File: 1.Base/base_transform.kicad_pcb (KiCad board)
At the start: 2 copper layers, 20 x 22.6 mm, 0 parts

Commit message: Updated Base File
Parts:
- added REF**: FBConnector, 1.Cookie.Board:FBConnector, F.Cu at (26.4, 23.8)
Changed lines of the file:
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@@
   )
   (net 0 "")
+  (footprint "1.Cookie.Board:FBConnector" (layer "F.Cu")
+    (at 26.35 23.79)
+    (fp_text reference "REF**" (at -0.02 9.21 unlocked) (layer "F.SilkS") hide
+        (effects (font (size 1 1) (thickness 0.1)))
+    )
+    (fp_text value "FBConnector" (at 0.36 13.61 unlocked) (layer "F.Fab") hide
+        (effects (font (size 1 1) (thickness 0.15)))
+    )
+    (fp_rect (start -0.1 -0.1) (end 0.1 0.1)
+      (stroke (width 0.01) (type solid)) (fill solid) (layer "F.Cu"))
+    (fp_rect (start -0.1 -0.1) (end 0.1 0.1)
+      (stroke (width 0.01) (type solid)) (fill solid) (layer "B.Cu"))
+    (pad "1" thru_hole circle (at 0 0) (size 0.1 0.1) (drill 0.1) (layers "*.Cu"))
+  )
   (gr_arc (start 26.83504 32.235) (mid 27.194224 32.383804) (end 27.34304 32.743)
     (stroke (width 0.1) (type solid)) (layer "F.Cu"))
@@
     )
     (stroke (width 0.1) (type solid)) (fill solid) (layer "F.Cu"))
-  (gr_arc (start 25.93 22.93) (mid 29.012419 27.568262) (end 30.552985 32.920032)
-    (stroke (width 0.5) (type solid)) (layer "F.Cu"))
   (gr_arc (start 32.44844 34.2416) (mid 32.299653 34.600824) (end 31.94044 34.7496)
     (stroke (width 0.1) (type solid)) (layer "F.Cu"))
@@
     )
     (stroke (width 0.1) (type solid)) (fill solid) (layer "B.Cu"))
+  (gr_line (start 26.35 23.79) (end 31 28.44)
+    (stroke (width 0.2) (type default)) (layer "B.Cu"))
   (gr_poly
     (pts
@@
   (gr_arc (start 13.014724 32.743379) (mid 13.163522 32.384177) (end 13.522724 32.235379)
     (stroke (width 0.1) (type solid)) (layer "B.Cu"))
+  (gr_line (start 31 28.44) (end 31 32.82)
+    (stroke (width 0.2) (type default)) (layer "B.Cu"))
   (gr_poly
     (pts
@@
     )
     (stroke (width 0.1) (type solid)) (fill solid) (layer "B.Cu"))
-  (gr_arc (start 26.255922 12.500319) (mid 22.70698 16.050122) (end 19.154081 12.504279)
-    (stroke (width 0.01) (type solid)) (layer "F.SilkS"))
   (gr_rect (start 12.435 32.085) (end 32.815 35.245)
     (stroke (width 0.01) (type solid)) (fill solid) (layer "B.Mask"))
-  (gr_rect (start 16.955 25.895) (end 26.455 16.095)
-    (stroke (width 0.01) (type solid)) (fill solid) (layer "F.Mask"))
-  (gr_rect (start 12.435 32.085) (end 32.815 35.245)
+  (gr_rect (start 12.61 12.47) (end 32.7 35.231967)
     (stroke (width 0.01) (type solid)) (fill solid) (layer "F.Mask"))
   (gr_line (start 29.4233 35.1052) (end 32.29604 35.1052)

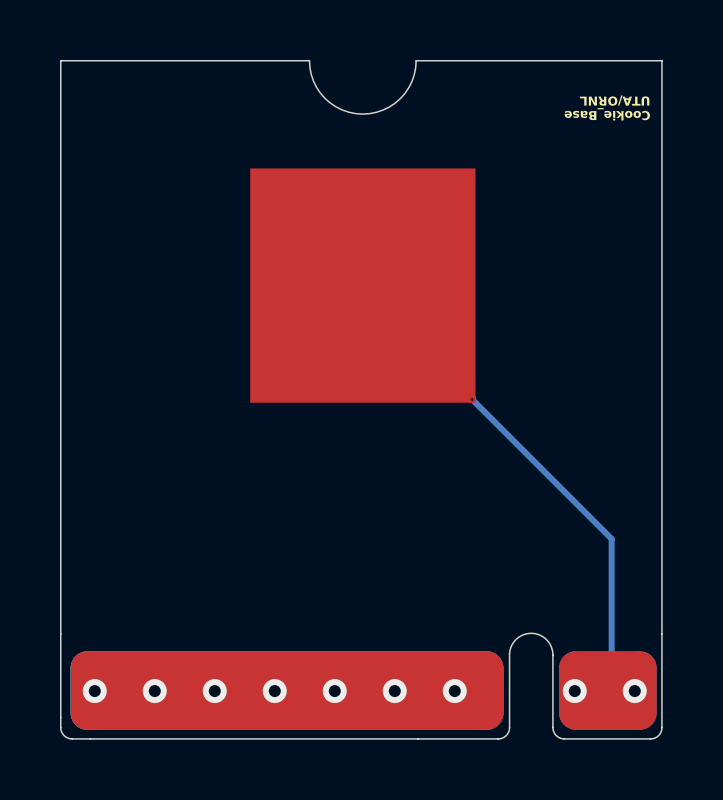
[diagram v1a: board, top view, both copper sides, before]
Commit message: Updated Collection pad to 6x6. Created new base
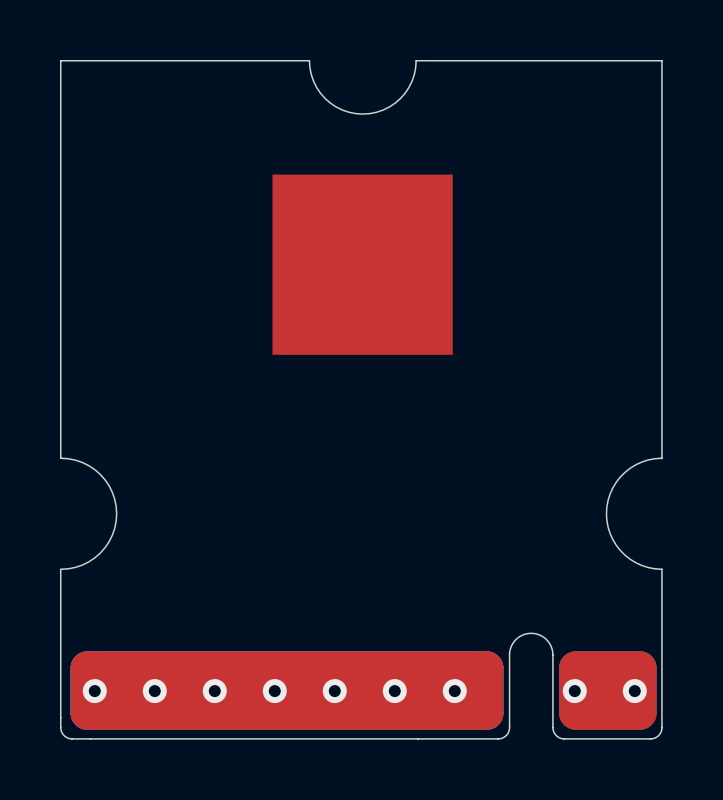
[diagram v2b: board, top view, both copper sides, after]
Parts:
- removed REF**: FBConnector, 1.Cookie.Board:FBConnector
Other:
- outline, holes or cut-outs redrawn
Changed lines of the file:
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@@
   )
   (net 0 "")
-  (footprint "1.Cookie.Board:FBConnector" (layer "F.Cu")
-    (at 26.35 23.79)
-    (fp_text reference "REF**" (at -0.02 9.21 unlocked) (layer "F.SilkS") hide
-        (effects (font (size 1 1) (thickness 0.1)))
-    )
-    (fp_text value "FBConnector" (at 0.36 13.61 unlocked) (layer "F.Fab") hide
-        (effects (font (size 1 1) (thickness 0.15)))
-    )
-    (fp_rect (start -0.1 -0.1) (end 0.1 0.1)
-      (stroke (width 0.01) (type solid)) (fill solid) (layer "F.Cu"))
-    (fp_rect (start -0.1 -0.1) (end 0.1 0.1)
-      (stroke (width 0.01) (type solid)) (fill solid) (layer "B.Cu"))
-    (pad "1" thru_hole circle (at 0 0) (size 0.1 0.1) (drill 0.1) (layers "*.Cu"))
-  )
   (gr_arc (start 26.83504 32.235) (mid 27.194224 32.383804) (end 27.34304 32.743)
     (stroke (width 0.1) (type solid)) (layer "F.Cu"))
@@
   (gr_arc (start 31.94044 32.235) (mid 32.299624 32.383804) (end 32.44844 32.743)
     (stroke (width 0.1) (type solid)) (layer "F.Cu"))
-  (gr_rect (start 18.955 16.095) (end 26.455 23.895)
+  (gr_rect (start 19.7 16.3) (end 25.7 22.3)
     (stroke (width 0.01) (type solid)) (fill solid) (layer "F.Cu"))
   (gr_arc (start 27.34304 34.2416) (mid 27.194253 34.600824) (end 26.83504 34.7496)
@@
     )
     (stroke (width 0.1) (type solid)) (fill solid) (layer "B.Cu"))
-  (gr_line (start 26.35 23.79) (end 31 28.44)
-    (stroke (width 0.2) (type default)) (layer "B.Cu"))
   (gr_poly
     (pts
@@
   (gr_arc (start 13.014724 32.743379) (mid 13.163522 32.384177) (end 13.522724 32.235379)
     (stroke (width 0.1) (type solid)) (layer "B.Cu"))
-  (gr_line (start 31 28.44) (end 31 32.82)
-    (stroke (width 0.2) (type default)) (layer "B.Cu"))
   (gr_poly
     (pts
@@
   (gr_line (start 13.01744 35.1052) (end 13.62704 35.1052)
     (stroke (width 0.05) (type solid)) (layer "Edge.Cuts"))
+  (gr_arc (start 32.67704 29.45) (mid 30.826843 27.599803) (end 32.67704 25.749606)
+    (stroke (width 0.05) (type default)) (layer "Edge.Cuts"))
   (gr_arc (start 29.4233 35.1052) (mid 29.153892 34.993608) (end 29.0423 34.7242)
     (stroke (width 0.05) (type solid)) (layer "Edge.Cuts"))
@@
   (gr_arc (start 24.483 12.4992) (mid 22.705 14.2772) (end 20.927 12.4992)
     (stroke (width 0.05) (type solid)) (layer "Edge.Cuts"))
-  (gr_line (start 32.67704 34.7242) (end 32.67704 31.6)
+  (gr_line (start 32.67704 34.7242) (end 32.67704 29.45)
     (stroke (width 0.05) (type solid)) (layer "Edge.Cuts"))
   (gr_line (start 12.63644 34.394) (end 12.63644 34.7242)
     (stroke (width 0.05) (type solid)) (layer "Edge.Cuts"))
-  (gr_line (start 32.67704 31.6) (end 32.67704 12.4992)
-    (stroke (width 0.05) (type solid)) (layer "Edge.Cuts"))
-  (gr_line (start 12.63644 34.394) (end 12.63644 31.6)
-    (stroke (width 0.05) (type solid)) (layer "Edge.Cuts"))
-  (gr_line (start 12.63644 31.6) (end 12.63644 12.4992)
-    (stroke (width 0.05) (type solid)) (layer "Edge.Cuts"))
-  (gr_rect (start 18.455 23.895) (end 18.955 24.395)
-    (stroke (width 0.01) (type default)) (fill none) (layer "User.8"))
-  (gr_rect (start 16.955 24.895) (end 17.955 24.895)
-    (stroke (width 0.01) (type default)) (fill none) (layer "User.8"))
-  (gr_rect (start 17.455 24.845) (end 17.955 24.895)
-    (stroke (width 0.01) (type default)) (fill none) (layer "User.8"))
-  (gr_rect (start 18.955 24.895) (end 26.455 25.395)
-    (stroke (width 0.01) (type default)) (fill none) (layer "User.8"))
-  (gr_rect (start 18.955 24.395) (end 26.455 24.895)
-    (stroke (width 0.01) (type default)) (fill none) (layer "User.8"))
+  (gr_line (start 32.67704 25.75) (end 32.67704 12.4992)
+    (stroke (width 0.05) (type solid)) (layer "Edge.Cuts"))
+  (gr_arc (start 12.65 25.749951) (mid 14.500049 27.6) (end 12.65 29.450049)
+    (stroke (width 0.05) (type default)) (layer "Edge.Cuts"))
+  (gr_line (start 12.63644 34.394) (end 12.63644 29.45)
+    (stroke (width 0.05) (type solid)) (layer "Edge.Cuts"))
+  (gr_line (start 12.63644 25.75) (end 12.63644 12.4992)
+    (stroke (width 0.05) (type solid)) (layer "Edge.Cuts"))
+  (gr_line (start 26.7 22.3) (end 26.7 16.3)
+    (stroke (width 0.01) (type dash)) (layer "User.8"))
+  (gr_rect (start 17.7 23.3) (end 18.7 24.3)
+    (stroke (width 0.01) (type solid)) (fill none) (layer "User.8"))
+  (gr_line (start 18.7 16.3) (end 18.7 22.3)
+    (stroke (width 0.01) (type dash)) (layer "User.8"))
+  (gr_rect (start 26.7 23.3) (end 27.7 24.3)
+    (stroke (width 0.01) (type solid)) (fill none) (layer "User.8"))
+  (gr_rect (start 19.7 16.3) (end 25.7 22.3)
+    (stroke (width 0.01) (type default)) (fill none) (layer "User.8"))
+  (gr_rect (start 18.2 14.8) (end 19.2 15.8)
+    (stroke (width 0.01) (type default)) (fill none) (layer "User.8"))
+  (gr_line (start 12.65 27.595) (end 32.65 27.595)
+    (stroke (width 0.01) (type default)) (layer "User.8"))
+  (gr_line (start 25.65 16.35) (end 27.2 14.8)
+    (stroke (width 0.01) (type default)) (layer "User.8"))
+  (gr_line (start 19.7 23.3) (end 25.7 23.3)
+    (stroke (width 0.01) (type dash)) (layer "User.8"))
+  (gr_rect (start 17.7 14.3) (end 18.7 15.3)
+    (stroke (width 0.01) (type solid)) (fill none) (layer "User.8"))
+  (gr_line (start 19.7 16.3) (end 18.2 14.8)
+    (stroke (width 0.01) (type default)) (layer "User.8"))
   (gr_line (start 22.705 14.295) (end 22.705 34.695)
     (stroke (width 0.01) (type default)) (layer "User.8"))
-  (gr_rect (start 17.955 24.895) (end 17.955 25.895)
-    (stroke (width 0.01) (type default)) (fill none) (layer "User.8"))
-  (gr_line (start 18.955 23.895) (end 16.955 25.895)
-    (stroke (width 0.01) (type default)) (layer "User.8"))
-  (gr_rect (start 17.955 16.095) (end 18.455 23.895)
-    (stroke (width 0.01) (type default)) (fill none) (layer "User.8"))
-  (gr_rect (start 17.455 23.895) (end 18.955 25.395)
-    (stroke (width 0.01) (type default)) (fill none) (layer "User.8"))
-  (gr_rect (start 16.955 24.895) (end 17.955 25.895)
-    (stroke (width 0.01) (type default)) (fill none) (layer "User.8"))
-  (gr_rect (start 17.955 24.895) (end 18.0004 25.395)
-    (stroke (width 0.01) (type default)) (fill none) (layer "User.8"))
-  (gr_rect (start 17.455 16.095) (end 17.955 23.895)
-    (stroke (width 0.01) (type default)) (fill none) (layer "User.8"))
-  (gr_line (start 12.635 12.495) (end 32.385 32.225)
-    (stroke (width 0.01) (type default)) (layer "User.8"))
-  (gr_rect (start 17.955 23.895) (end 18.955 24.895)
-    (stroke (width 0.01) (type default)) (fill none) (layer "User.8"))
-  (gr_text "Cookie_Base\nUTA/ORNL\n" (at 32.29604 14.074 180) (layer "F.SilkS")
-    (effects (font (size 0.3 0.3) (thickness 0.075) bold) (justify left))
+  (gr_line (start 19.2 15.8) (end 26.2 15.8)
+    (stroke (width 0.01) (type default)) (layer "User.8"))
+  (gr_line (start 18.7 22.8) (end 26.7 22.8)
+    (stroke (width 0.01) (type default)) (layer "User.8"))
+  (gr_rect (start 18.7 22.3) (end 19.7 23.3)
+    (stroke (width 0.01) (type default)) (fill none) (layer "User.8"))
+  (gr_line (start 25.7 22.3) (end 27.2 23.8)
+    (stroke (width 0.01) (type default)) (layer "User.8"))
+  (gr_rect (start 18.7 15.3) (end 19.7 16.3)
+    (stroke (width 0.01) (type default)) (fill none) (layer "User.8"))
+  (gr_line (start 25.7 15.3) (end 19.7 15.3)
+    (stroke (width 0.01) (type dash)) (layer "User.8"))
+  (gr_rect (start 25.7 15.3) (end 26.7 16.3)
+    (stroke (width 0.01) (type default)) (fill none) (layer "User.8"))
+  (gr_rect (start 26.2 14.8) (end 27.2 15.8)
+    (stroke (width 0.01) (type default)) (fill none) (layer "User.8"))
+  (gr_line (start 26.2 22.8) (end 26.2 15.8)
+    (stroke (width 0.01) (type default)) (layer "User.8"))
+  (gr_line (start 19.7 22.3) (end 18.2 23.8)
+    (stroke (width 0.01) (type default)) (layer "User.8"))
+  (gr_rect (start 18.2 22.8) (end 19.2 23.8)
+    (stroke (width 0.01) (type default)) (fill none) (layer "User.8"))
+  (gr_rect (start 26.2 22.8) (end 27.2 23.8)
+    (stroke (width 0.01) (type default)) (fill none) (layer "User.8"))
+  (gr_rect (start 26.7 14.3) (end 27.7 15.3)
+    (stroke (width 0.01) (type solid)) (fill none) (layer "User.8"))
+  (gr_rect (start 25.7 22.3) (end 26.7 23.3)
+    (stroke (width 0.01) (type default)) (fill none) (layer "User.8"))
+  (gr_line (start 19.2 15.8) (end 19.2 22.8)
+    (stroke (width 0.01) (type default)) (layer "User.8"))
+  (gr_rect (start 26.2 15.3) (end 26.7 15.8)
+    (stroke (width 0.01) (type default)) (fill none) (layer "User.8"))
+  (gr_text "Cookie_Base\nUTA/ORNL\n" (at 29.55 13.2 180) (layer "B.SilkS")
+    (effects (font (size 0.3 0.3) (thickness 0.075) bold) (justify left mirror))
   )
   (via (at 31.77104 33.51) (size 0.8) (drill 0.4) (layers "F.Cu" "B.Cu") (net 0))
